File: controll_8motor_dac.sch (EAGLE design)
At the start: 60 parts

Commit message: DCジャックを長穴＆外向きにした
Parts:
- removed DC-JACK: (no value), BD6211F:JACK-PLUG0
- added U$1: 2.1MMJACKTHM, adafruit:2.1MMJACKTHM
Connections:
- net N$97: now also U$1.TIP; no longer DC-JACK.3
- net P-DIORD1: now also U$1.RING; no longer DC-JACK.1

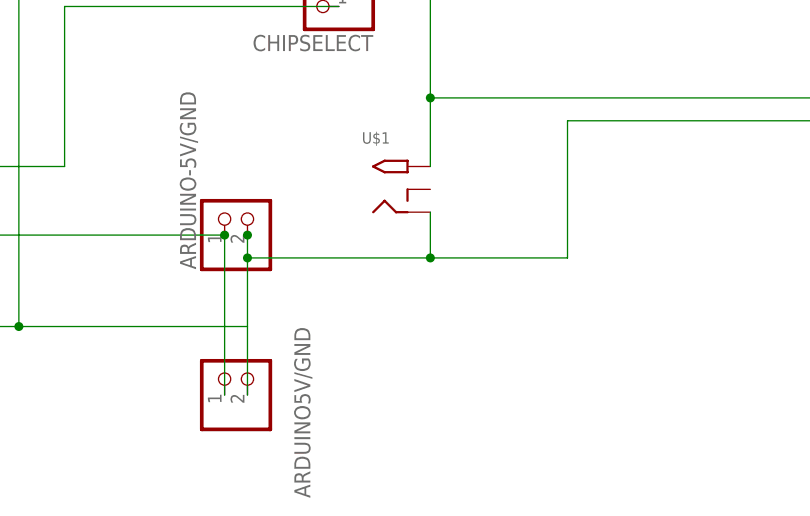
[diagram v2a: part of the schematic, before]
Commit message: 基板加工機の使い方を間違えていたことに気づいたので DCジャックのつなぎ方を戻した． さらに，このまま掘ってしまうと表面実装がミラーになってしまうのでこれから 修正する
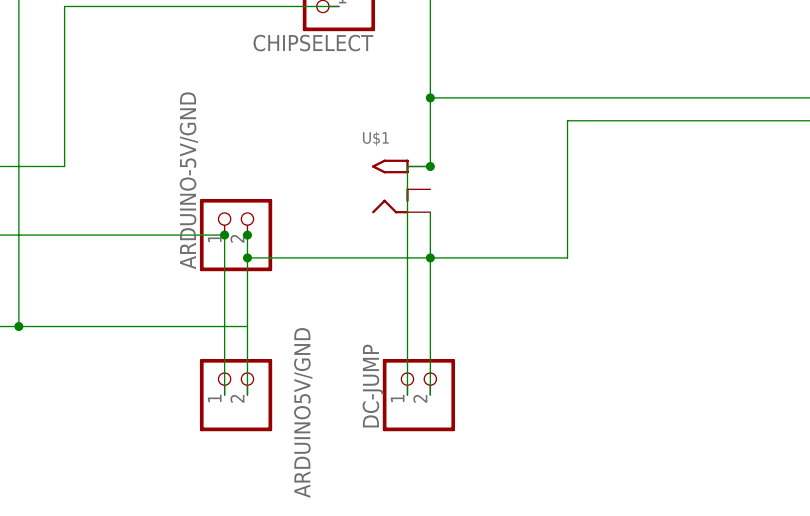
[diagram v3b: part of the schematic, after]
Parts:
- added DC-JUMP: (no value), pinhead:PINHD-1X2
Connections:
- net N$97: now also DC-JUMP.1
- net P-DIORD1: now also DC-JUMP.2
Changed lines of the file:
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@@
 <part name="M-DRIVER_5" library="BD6211F" deviceset="BD6211F-E2" device=""/>
 <part name="U$1" library="adafruit" deviceset="2.1MMJACK" device="THM"/>
+<part name="DC-JUMP" library="pinhead" library_urn="urn:adsk.eagle:library:325" deviceset="PINHD-1X2" device="" package3d_urn="urn:adsk.eagle:package:22435/2"/>
 </parts>
 <sheets>
@@
 <instance part="U$1" gate="G$1" x="38.1" y="96.52" smashed="yes">
 <attribute name="NAME" x="35.56" y="101.6" size="1.27" layer="95"/>
+</instance>
+<instance part="DC-JUMP" gate="G$1" x="43.18" y="76.2" smashed="yes" rot="R90">
+<attribute name="NAME" x="37.465" y="69.85" size="1.778" layer="95" rot="R90"/>
+<attribute name="VALUE" x="48.26" y="69.85" size="1.778" layer="96" rot="R90"/>
 </instance>
 </instances>
@@
 <wire x1="43.18" y1="106.68" x2="43.18" y2="99.06" width="0.1524" layer="91"/>
 <junction x="43.18" y="106.68"/>
+<pinref part="DC-JUMP" gate="G$1" pin="1"/>
+<wire x1="40.64" y1="73.66" x2="40.64" y2="99.06" width="0.1524" layer="91"/>
+<wire x1="40.64" y1="99.06" x2="43.18" y2="99.06" width="0.1524" layer="91"/>
+<junction x="43.18" y="99.06"/>
 </segment>
 </net>
@@
 <wire x1="43.18" y1="93.98" x2="43.18" y2="88.9" width="0.1524" layer="91"/>
 <junction x="43.18" y="88.9"/>
-</segment>
-</net>
+<pinref part="DC-JUMP" gate="G$1" pin="2"/>
+<wire x1="43.18" y1="88.9" x2="43.18" y2="73.66" width="0.1524" layer="91"/>
+</segment>
+</net>

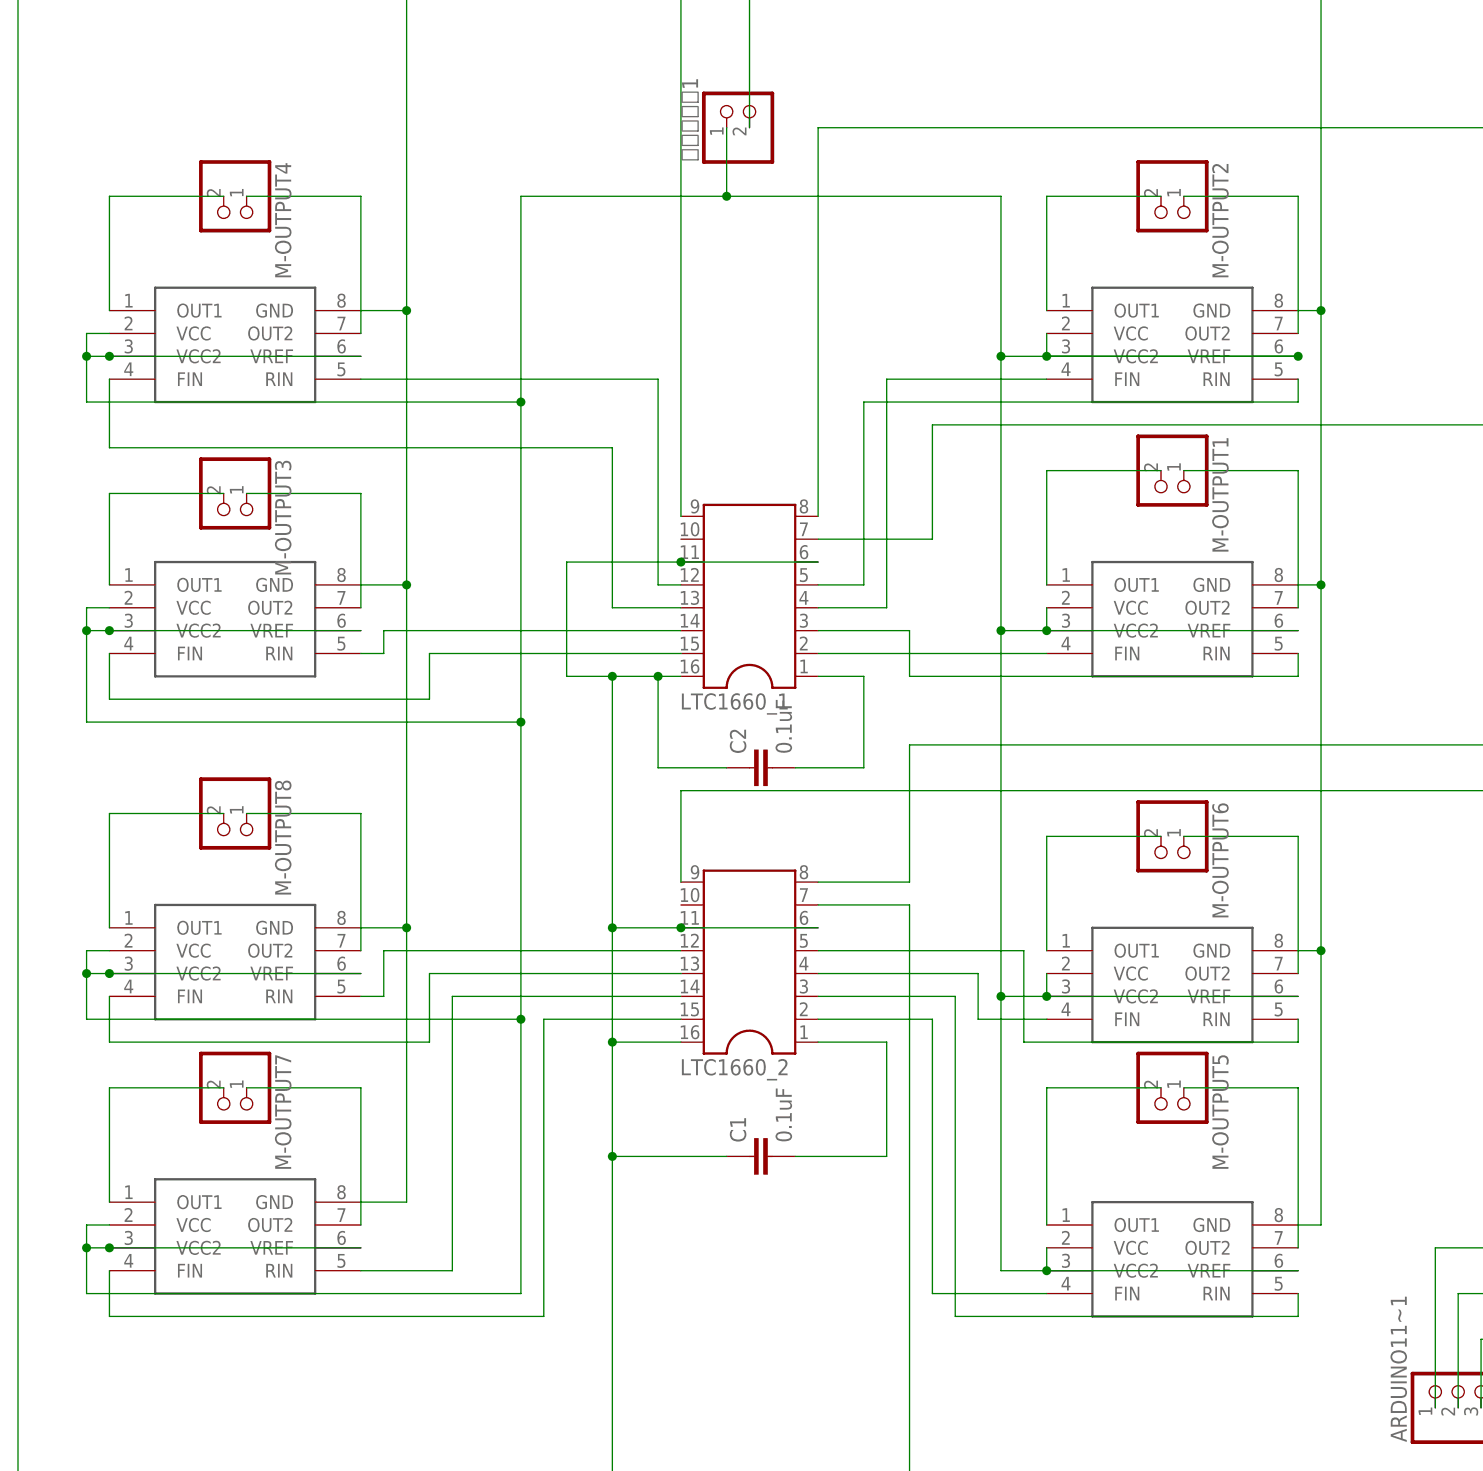
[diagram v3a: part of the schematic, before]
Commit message: 変換基盤を乗せるバージョン．(まだ微妙に刺さらない) - モータドライバ壊れた時ように変換基盤付けたほうがよいよというアドバイスを受けて
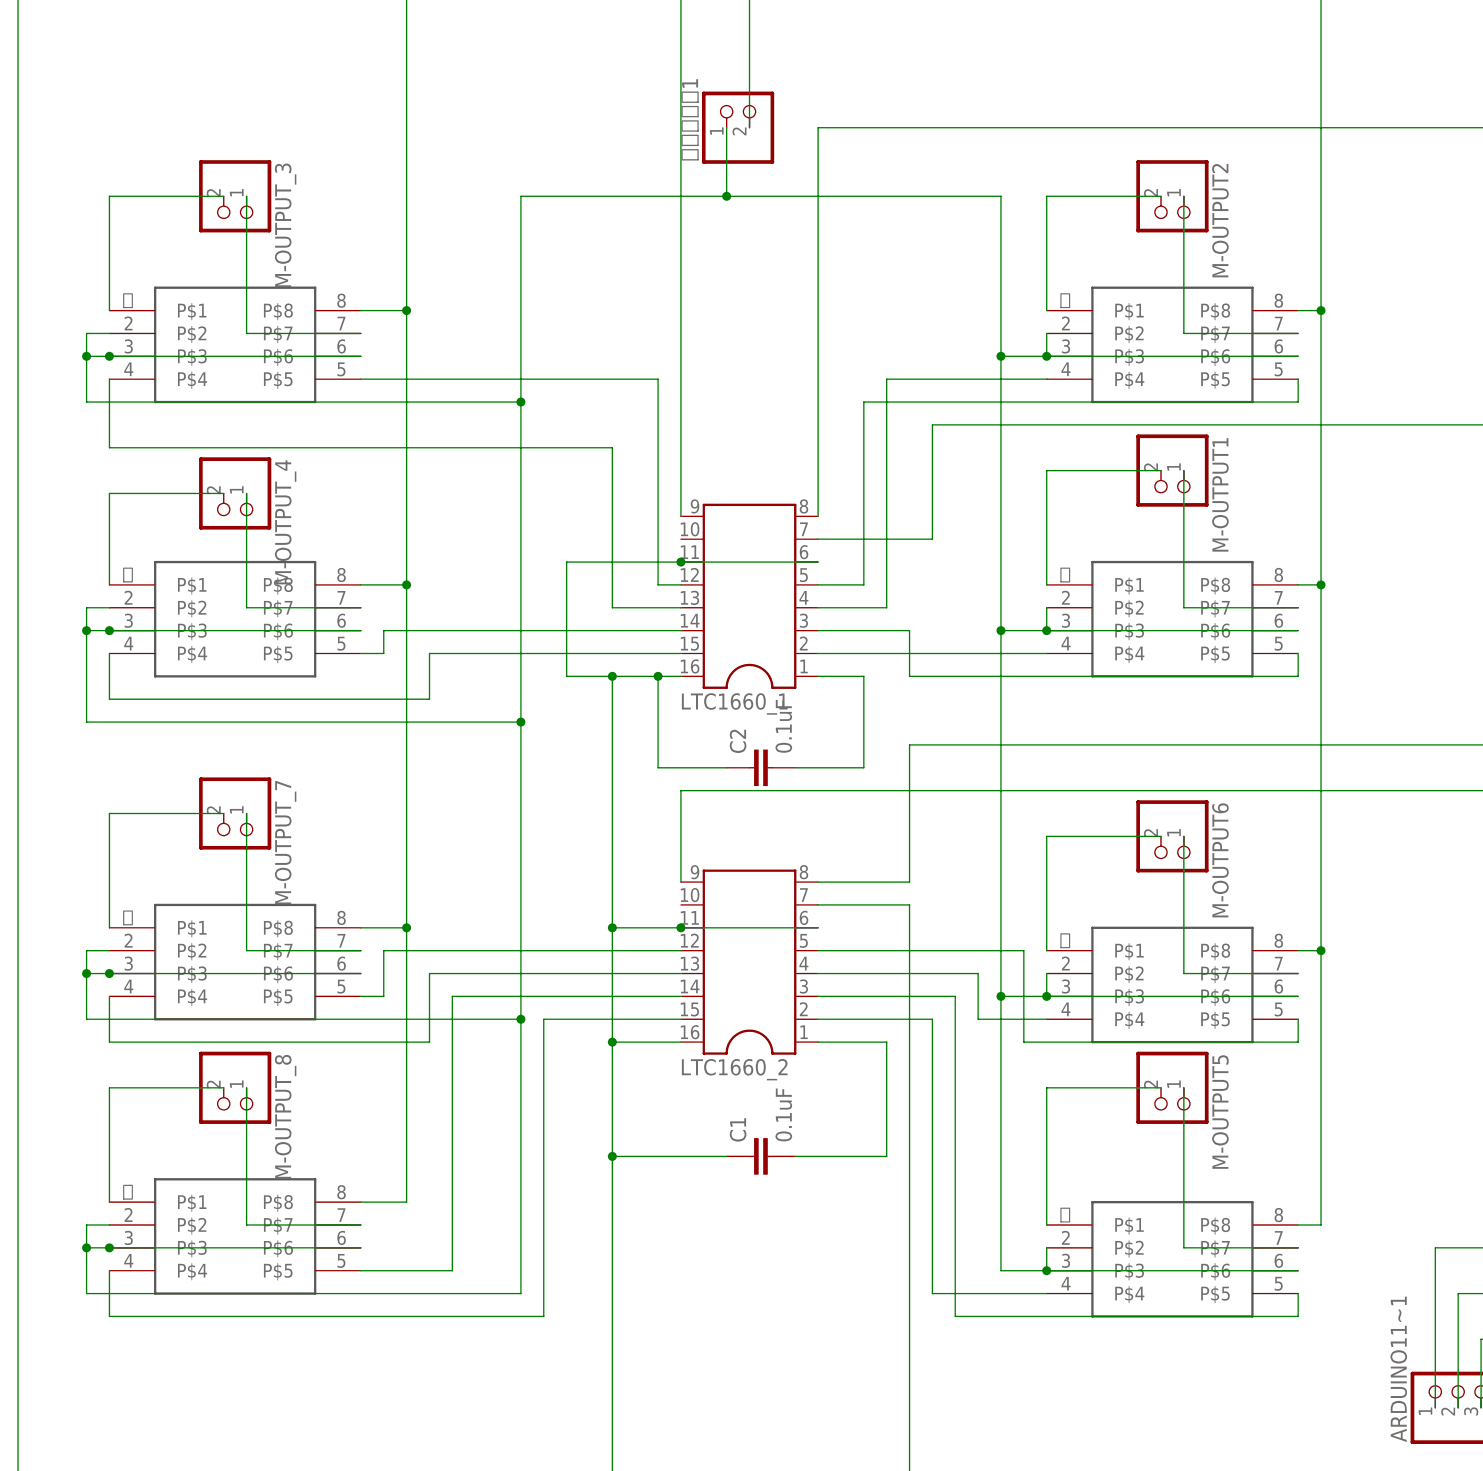
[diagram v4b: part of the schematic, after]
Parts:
- removed M-DRIVER_1, M-DRIVER_2, M-DRIVER_3, M-DRIVER_4, M-DRIVER_5, M-DRIVER_6, M-DRIVER_7, M-DRIVER_8: BD6211F-E2, BD6211F:BD6211F-E2
- added M-DRIVER1, M-DRIVER2, M-DRIVER3, M-DRIVER4, M-DRIVER5, M-DRIVER6, M-DRIVER7, M-DRIVER8: SOP8-DIP-CONVERTER, SOP8-DIP-Converter:SOP8-DIP-CONVERTER
- renumbered M-OUTPUT3 to M-OUTPUT_4, M-OUTPUT4 to M-OUTPUT_3, M-OUTPUT7 to M-OUTPUT_8, M-OUTPUT8 to M-OUTPUT_7
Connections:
- net N$1: now also M-DRIVER3.P$5; no longer M-DRIVER_4.RIN
- net N$10: now also M-DRIVER2.P$4; no longer M-DRIVER_2.FIN
- net N$11: now also M-DRIVER1.P$5; no longer M-DRIVER_1.RIN
- net N$12: now also M-DRIVER1.P$4; no longer M-DRIVER_1.FIN
- net N$13: now also M-DRIVER5.P$1; no longer M-DRIVER_5.OUT1
- net N$14: now also M-DRIVER6.P$4; no longer M-DRIVER_6.FIN
- net N$15: now also M-DRIVER5.P$5; no longer M-DRIVER_5.RIN
- net N$16: now also M-DRIVER5.P$4; no longer M-DRIVER_5.FIN
- net N$17: now also M-DRIVER3.P$7; no longer M-DRIVER_4.OUT2
- net N$18: now also M-DRIVER4.P$7; no longer M-DRIVER_3.OUT2
- net N$19: now also M-DRIVER4.P$1; no longer M-DRIVER_3.OUT1
- net N$2: now also M-DRIVER3.P$1; no longer M-DRIVER_4.OUT1
- net N$20: now also M-DRIVER7.P$7; no longer M-DRIVER_8.OUT2
- net N$21: now also M-DRIVER7.P$1; no longer M-DRIVER_8.OUT1
- net N$22: now also M-DRIVER8.P$7; no longer M-DRIVER_7.OUT2
- net N$23: now also M-DRIVER8.P$1; no longer M-DRIVER_7.OUT1
- net N$24: now also M-DRIVER1.P$7; no longer M-DRIVER_1.OUT2
- net N$26: now also M-DRIVER4.P$5; no longer M-DRIVER_3.RIN
- net N$27: now also M-DRIVER2.P$7; no longer M-DRIVER_2.OUT2
- net N$28: now also M-DRIVER2.P$1; no longer M-DRIVER_2.OUT1
- net N$29: now also M-DRIVER6.P$5; no longer M-DRIVER_6.RIN
- net N$3: now also M-DRIVER3.P$4; no longer M-DRIVER_4.FIN
- net N$30: now also M-DRIVER5.P$7; no longer M-DRIVER_5.OUT2
- net N$31: now also M-DRIVER6.P$1; no longer M-DRIVER_6.OUT1
- net N$32: now also M-DRIVER6.P$7; no longer M-DRIVER_6.OUT2
- net N$33: now also M-DRIVER1.P$2, M-DRIVER1.P$3, M-DRIVER1.P$6, M-DRIVER2.P$2, M-DRIVER2.P$3, M-DRIVER2.P$6, M-DRIVER3.P$2, M-DRIVER3.P$3, M-DRIVER3.P$6, M-DRIVER4.P$2, M-DRIVER4.P$3, M-DRIVER4.P$6, M-DRIVER5.P$2, M-DRIVER5.P$3, M-DRIVER5.P$6, M-DRIVER6.P$2, M-DRIVER6.P$3, M-DRIVER6.P$6, M-DRIVER7.P$2, M-DRIVER7.P$3, M-DRIVER7.P$6, M-DRIVER8.P$2, M-DRIVER8.P$3, M-DRIVER8.P$6; no longer M-DRIVER_1.VCC, M-DRIVER_1.VCC2, M-DRIVER_1.VREF, M-DRIVER_2.VCC, M-DRIVER_2.VCC2, M-DRIVER_2.VREF, M-DRIVER_3.VCC, M-DRIVER_3.VCC2, M-DRIVER_3.VREF, M-DRIVER_4.VCC, M-DRIVER_4.VCC2, M-DRIVER_4.VREF, M-DRIVER_5.VCC, M-DRIVER_5.VCC2, M-DRIVER_5.VREF, M-DRIVER_6.VCC, M-DRIVER_6.VCC2, M-DRIVER_6.VREF, M-DRIVER_7.VCC, M-DRIVER_7.VCC2, M-DRIVER_7.VREF, M-DRIVER_8.VCC, M-DRIVER_8.VCC2, M-DRIVER_8.VREF
- net N$4: now also M-DRIVER4.P$4; no longer M-DRIVER_3.FIN
- net N$40: now also M-DRIVER1.P$1; no longer M-DRIVER_1.OUT1
- net N$5: now also M-DRIVER7.P$5; no longer M-DRIVER_8.RIN
- net N$6: now also M-DRIVER7.P$4; no longer M-DRIVER_8.FIN
- net N$7: now also M-DRIVER8.P$5; no longer M-DRIVER_7.RIN
- net N$8: now also M-DRIVER8.P$4; no longer M-DRIVER_7.FIN
- net N$9: now also M-DRIVER2.P$5; no longer M-DRIVER_2.RIN
- net P-DIORD1: now also M-DRIVER1.P$8, M-DRIVER2.P$8, M-DRIVER3.P$8, M-DRIVER4.P$8, M-DRIVER5.P$8, M-DRIVER6.P$8, M-DRIVER7.P$8, M-DRIVER8.P$8; no longer M-DRIVER_1.GND, M-DRIVER_2.GND, M-DRIVER_3.GND, M-DRIVER_4.GND, M-DRIVER_5.GND, M-DRIVER_6.GND, M-DRIVER_7.GND, M-DRIVER_8.GND

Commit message: 配線してみた,icパーツ使ってみた
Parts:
- M-DRIVER1, M-DRIVER2, M-DRIVER3, M-DRIVER4, M-DRIVER5, M-DRIVER6, M-DRIVER7, M-DRIVER8: value SOP8-DIP-CONVERTER -> (none); device SOP8-DIP-Converter:SOP8-DIP-CONVERTER -> ic-package:DIL8S
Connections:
- net N$1: now also M-DRIVER3.5; no longer M-DRIVER3.P$5
- net N$10: now also M-DRIVER2.4; no longer M-DRIVER2.P$4
- net N$11: now also M-DRIVER1.5; no longer M-DRIVER1.P$5
- net N$12: now also M-DRIVER1.4; no longer M-DRIVER1.P$4
- net N$13: now also M-DRIVER5.1; no longer M-DRIVER5.P$1
- net N$14: now also M-DRIVER6.4; no longer M-DRIVER6.P$4
- net N$15: now also M-DRIVER5.5; no longer M-DRIVER5.P$5
- net N$16: now also M-DRIVER5.4; no longer M-DRIVER5.P$4
- net N$17: now also M-DRIVER3.7; no longer M-DRIVER3.P$7
- net N$18: now also M-DRIVER4.7; no longer M-DRIVER4.P$7
- net N$19: now also M-DRIVER4.1; no longer M-DRIVER4.P$1
- net N$2: now also M-DRIVER3.1; no longer M-DRIVER3.P$1
- net N$20: now also M-DRIVER7.7; no longer M-DRIVER7.P$7
- net N$21: now also M-DRIVER7.1; no longer M-DRIVER7.P$1
- net N$22: now also M-DRIVER8.7; no longer M-DRIVER8.P$7
- net N$23: now also M-DRIVER8.1; no longer M-DRIVER8.P$1
- net N$24: now also M-DRIVER1.7; no longer M-DRIVER1.P$7
- net N$26: now also M-DRIVER4.5; no longer M-DRIVER4.P$5
- net N$27: now also M-DRIVER2.7; no longer M-DRIVER2.P$7
- net N$28: now also M-DRIVER2.1; no longer M-DRIVER2.P$1
- net N$29: now also M-DRIVER6.5; no longer M-DRIVER6.P$5
- net N$3: now also M-DRIVER3.4; no longer M-DRIVER3.P$4
- net N$30: now also M-DRIVER5.7; no longer M-DRIVER5.P$7
- net N$31: now also M-DRIVER6.1; no longer M-DRIVER6.P$1
- net N$32: now also M-DRIVER6.7; no longer M-DRIVER6.P$7
- net N$33: now also M-DRIVER1.2, M-DRIVER1.3, M-DRIVER1.6, M-DRIVER2.2, M-DRIVER2.3, M-DRIVER2.6, M-DRIVER3.2, M-DRIVER3.3, M-DRIVER3.6, M-DRIVER4.2, M-DRIVER4.3, M-DRIVER4.6, M-DRIVER5.2, M-DRIVER5.3, M-DRIVER5.6, M-DRIVER6.2, M-DRIVER6.3, M-DRIVER6.6, M-DRIVER7.2, M-DRIVER7.3, M-DRIVER7.6, M-DRIVER8.2, M-DRIVER8.3, M-DRIVER8.6; no longer M-DRIVER1.P$2, M-DRIVER1.P$3, M-DRIVER1.P$6, M-DRIVER2.P$2, M-DRIVER2.P$3, M-DRIVER2.P$6, M-DRIVER3.P$2, M-DRIVER3.P$3, M-DRIVER3.P$6, M-DRIVER4.P$2, M-DRIVER4.P$3, M-DRIVER4.P$6, M-DRIVER5.P$2, M-DRIVER5.P$3, M-DRIVER5.P$6, M-DRIVER6.P$2, M-DRIVER6.P$3, M-DRIVER6.P$6, M-DRIVER7.P$2, M-DRIVER7.P$3, M-DRIVER7.P$6, M-DRIVER8.P$2, M-DRIVER8.P$3, M-DRIVER8.P$6
- net N$4: now also M-DRIVER4.4; no longer M-DRIVER4.P$4
- net N$40: now also M-DRIVER1.1; no longer M-DRIVER1.P$1
- net N$5: now also M-DRIVER7.5; no longer M-DRIVER7.P$5
- net N$6: now also M-DRIVER7.4; no longer M-DRIVER7.P$4
- net N$7: now also M-DRIVER8.5; no longer M-DRIVER8.P$5
- net N$8: now also M-DRIVER8.4; no longer M-DRIVER8.P$4
- net N$9: now also M-DRIVER2.5; no longer M-DRIVER2.P$5
- net P-DIORD1: now also M-DRIVER1.8, M-DRIVER2.8, M-DRIVER3.8, M-DRIVER4.8, M-DRIVER5.8, M-DRIVER6.8, M-DRIVER7.8, M-DRIVER8.8; no longer M-DRIVER1.P$8, M-DRIVER2.P$8, M-DRIVER3.P$8, M-DRIVER4.P$8, M-DRIVER5.P$8, M-DRIVER6.P$8, M-DRIVER7.P$8, M-DRIVER8.P$8
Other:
- moved on the sheet: M-OUTPUT1, M-OUTPUT2, M-OUTPUT5, M-OUTPUT6, M-OUTPUT_3, M-OUTPUT_4, M-OUTPUT_7, M-OUTPUT_8

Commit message: 配線しなおし
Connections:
- removed net N$34: C2.2, LTC1660_1.1
- removed net N$35: C1.2, LTC1660_2.1
- removed net P-DIORD1: ARDUINO-5V/GND.2, ARDUINO5V/GND.2, DC-JUMP.2, M-DRIVER1.8, M-DRIVER2.8, M-DRIVER3.8, M-DRIVER4.8, M-DRIVER5.8, M-DRIVER6.8, M-DRIVER7.8, M-DRIVER8.8, MCP3208‐1.14, MCP3208‐1.9, P-DIODE1.1, P-DIODE2.1, P-DIODE3.1, P-DIODE4.1, P-DIODE5.1, P-DIODE6.1, P-DIODE7.1, P-DIODE8.1, R1.1, R11.1, R13.1, R15.1, R3.1, R5.1, R7.1, R9.1, U$1.RING, 安定化電源1.2
- new net GND: ARDUINO-5V/GND.2, ARDUINO5V/GND.2, C1.2, C2.2, DC-JUMP.2, LTC1660_1.1, LTC1660_2.1, M-DRIVER1.8, M-DRIVER2.8, M-DRIVER3.8, M-DRIVER4.8, M-DRIVER5.8, M-DRIVER6.8, M-DRIVER7.8, M-DRIVER8.8, MCP3208‐1.14, MCP3208‐1.9, P-DIODE1.1, P-DIODE2.1, P-DIODE3.1, P-DIODE4.1, P-DIODE5.1, P-DIODE6.1, P-DIODE7.1, P-DIODE8.1, R1.1, R11.1, R13.1, R15.1, R3.1, R5.1, R7.1, R9.1, U$1.RING, 安定化電源1.2
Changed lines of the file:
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@@
 <?xml version="1.0" encoding="utf-8"?>
 <!DOCTYPE eagle SYSTEM "eagle.dtd">
-<eagle version="9.5.0">
+<eagle version="9.3.2">
 <drawing>
 <settings>
@@
 <setting verticaltext="up"/>
 </settings>
-<grid distance="0.1" unitdist="inch" unit="mm" style="lines" multiple="1" display="yes" altdistance="0.01" altunitdist="inch" altunit="mm"/>
+<grid distance="0.1" unitdist="inch" unit="inch" style="lines" multiple="1" display="no" altdistance="0.01" altunitdist="inch" altunit="inch"/>
 <layers>
 <layer number="1" name="Top" color="4" fill="1" visible="no" active="no"/>
@@
 </segment>
 </net>
-<net name="N$34" class="0">
-<segment>
-<pinref part="LTC1660_1" gate="G$1" pin="1"/>
-<wire x1="-121.92" y1="195.58" x2="-116.84" y2="195.58" width="0.1524" layer="91"/>
-<wire x1="-116.84" y1="195.58" x2="-116.84" y2="185.42" width="0.1524" layer="91"/>
-<pinref part="C2" gate="G$1" pin="2"/>
-<wire x1="-116.84" y1="185.42" x2="-124.46" y2="185.42" width="0.1524" layer="91"/>
-</segment>
-</net>
-<net name="N$35" class="0">
-<segment>
-<pinref part="LTC1660_2" gate="G$1" pin="1"/>
-<wire x1="-121.92" y1="154.94" x2="-114.3" y2="154.94" width="0.1524" layer="91"/>
-<wire x1="-114.3" y1="154.94" x2="-114.3" y2="142.24" width="0.1524" layer="91"/>
-<pinref part="C1" gate="G$1" pin="2"/>
-<wire x1="-114.3" y1="142.24" x2="-124.46" y2="142.24" width="0.1524" layer="91"/>
-</segment>
-</net>
 <net name="N$38" class="0">
 <segment>
@@
 </segment>
 </net>
-<net name="P-DIORD1" class="0">
+<net name="GND" class="0">
 <segment>
 <pinref part="P-DIODE1" gate="G$1" pin="1"/>
@@
 <wire x1="-66.04" y1="284.48" x2="-129.54" y2="284.48" width="0.1524" layer="91"/>
 <wire x1="-66.04" y1="236.22" x2="-66.04" y2="205.74" width="0.1524" layer="91"/>
-<wire x1="-66.04" y1="205.74" x2="-66.04" y2="165.1" width="0.1524" layer="91"/>
+<wire x1="-66.04" y1="205.74" x2="-66.04" y2="190.5" width="0.1524" layer="91"/>
 <pinref part="U$1" gate="G$1" pin="RING"/>
-<wire x1="-66.04" y1="165.1" x2="-66.04" y2="134.62" width="0.1524" layer="91"/>
+<wire x1="-66.04" y1="190.5" x2="-66.04" y2="165.1" width="0.1524" layer="91"/>
+<wire x1="-66.04" y1="165.1" x2="-66.04" y2="144.78" width="0.1524" layer="91"/>
+<wire x1="-66.04" y1="144.78" x2="-66.04" y2="134.62" width="0.1524" layer="91"/>
 <wire x1="43.18" y1="93.98" x2="43.18" y2="88.9" width="0.1524" layer="91"/>
 <junction x="43.18" y="88.9"/>
@@
 <wire x1="-185.42" y1="167.64" x2="-167.64" y2="167.64" width="0.1524" layer="91"/>
 <junction x="-167.64" y="167.64"/>
-</segment>
-</net>
+<pinref part="LTC1660_1" gate="G$1" pin="1"/>
+<wire x1="-121.92" y1="195.58" x2="-116.84" y2="195.58" width="0.1524" layer="91"/>
+<wire x1="-116.84" y1="195.58" x2="-116.84" y2="190.5" width="0.1524" layer="91"/>
+<pinref part="C2" gate="G$1" pin="2"/>
+<wire x1="-116.84" y1="190.5" x2="-116.84" y2="185.42" width="0.1524" layer="91"/>
+<wire x1="-116.84" y1="185.42" x2="-124.46" y2="185.42" width="0.1524" layer="91"/>
+<wire x1="-116.84" y1="190.5" x2="-66.04" y2="190.5" width="0.1524" layer="91"/>
+<junction x="-116.84" y="190.5"/>
+<junction x="-66.04" y="190.5"/>
+<label x="-66.04" y="193.04" size="1.778" layer="95"/>
+<pinref part="LTC1660_2" gate="G$1" pin="1"/>
+<wire x1="-121.92" y1="154.94" x2="-114.3" y2="154.94" width="0.1524" layer="91"/>
+<wire x1="-114.3" y1="154.94" x2="-114.3" y2="144.78" width="0.1524" layer="91"/>
+<pinref part="C1" gate="G$1" pin="2"/>
+<wire x1="-114.3" y1="144.78" x2="-114.3" y2="142.24" width="0.1524" layer="91"/>
+<wire x1="-114.3" y1="142.24" x2="-124.46" y2="142.24" width="0.1524" layer="91"/>
+<wire x1="-114.3" y1="144.78" x2="-66.04" y2="144.78" width="0.1524" layer="91"/>
+<junction x="-114.3" y="144.78"/>
+<junction x="-66.04" y="144.78"/>
+</segment>
+</net>
